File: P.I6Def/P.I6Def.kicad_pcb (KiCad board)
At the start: 2 copper layers, 48.9 x 70.8 mm, 41 parts, among them J1 B3B-PH-K-S, J2 B3B-PH-K-S, J3 CX90B-16P1, J4 B4B-PH-SM4-TB_LF__SN__P_, J5 B4B-PH-SM4-TB_LF__SN__P_, SW2 SW_SPST, SW3 SW_SPST, U2 LMV321IDCKT, U3 LMV321IDCKT, U4 LMV321IDCKT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

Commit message: MEJORA DE LA PCB
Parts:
- removed X1: ESP32-S3-WROOM-1-N16R8, ESP32-S3-WROOM-1-N16R8:ESP32S3WROOM1N8R2
- added U6: ESP32-S3-WROOM-1, RF_Module:ESP32-S3-WROOM-1U, F.Cu at (126.8, 93.2)
- moved C6 70.7 mm to (142.3, 81.1), turned to 180 degrees
- moved C16 65.1 mm to (139.0, 72.7)
- moved R7 60.4 mm to (142.2, 78.3), turned to 180 degrees
- moved C9 56.9 mm to (130.6, 72.0), turned to 90 degrees
- moved R8 51.5 mm to (132.9, 72.0), turned to 90 degrees
- moved C11 38.4 mm to (139.3, 98.4), turned to 0 degrees
- moved C5 37.8 mm to (139.4, 100.7), turned to 0 degrees
- moved R11 35.5 mm to (112.7, 96.9)
- moved R10 33.8 mm to (113.3, 80.6), turned to -90 degrees
- moved R9 30.1 mm to (111.2, 80.6), turned to -90 degrees
- moved SW3 19.1 mm to (123.1, 72.4), turned to 180 degrees
- moved J2 8.78 mm to (106.9, 70.0)
- moved J4 5.52 mm to (104.3, 82.3)
- moved J5 5.16 mm to (104.3, 95.8)
- moved SW2 3.30 mm to (142.5, 89.3), turned to -90 degrees
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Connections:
- net Net-(SW3-A) renamed /BOOT
- C1 pad 1: VBUS_B -> +5V
- C2 pad 1: VBUS_B -> +5V
- J3 pad B4: VBUS_B -> +5V
- J3 pad B9: VBUS_B -> +5V
- VR1 pad 1: VBUS_B -> +5V
- VR1 pad 4: VBUS_B -> +5V
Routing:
- net +3.3V: track 39.2 -> 164.0 mm, vias 1 -> 10
- net GND: track 109.2 -> 42.5 mm, vias 1 -> 3
- net /D-: track 0.00 -> 47.9 mm, vias 0 -> 4
- net /ADC1_CH1: track 1.92 -> 47.1 mm, vias 0 -> 2
- net /ADC1_CH0: track 0.00 -> 45.0 mm, vias 0 -> 4
- net /D+: track 0.00 -> 44.7 mm, vias 0 -> 4
- net Net-(SW2-A): track 0.00 -> 29.4 mm
- net +5V: track 47.4 -> 74.4 mm, vias 1 -> 2
- net /BOOT: track 0.00 -> 25.3 mm
- net /SCL_CSS811: track 0.00 -> 21.3 mm
- net VBUS_B: track 20.5 -> 0.00 mm
- net /SDA_CSS811: track 0.00 -> 19.5 mm, vias 0 -> 2
- net /ADDR_CCS811: track 0.00 -> 14.1 mm
- net /WAKE_CCS811: track 0.00 -> 12.2 mm
- net /nINT_CCS811: track 0.00 -> 11.8 mm
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- added copper zone on B.Cu, net GND
- added copper zone on F.Cu, net GND
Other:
- board size 48.9 x 70.8 mm -> 46.3 x 60.2 mm

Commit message: Actualizacion PCB
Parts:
- moved R11 1.53 mm to (112.4, 95.4)
- moved R12 0.90 mm to (121.7, 55.0)
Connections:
- U6 pad 17: unconnected-(U6-IO9-Pad17) -> /ADC1_CH0
- U6 pad 18: unconnected-(U6-IO10-Pad18) -> /ADC1_CH1
- U6 pad 4: /ADC1_CH1 -> unconnected-(U6-IO4-Pad4)
- U6 pad 5: /ADC1_CH0 -> unconnected-(U6-IO5-Pad5)
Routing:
- net GND: track 42.5 -> 73.2 mm, vias 3 -> 6
- net /ADC1_CH0: track 45.0 -> 25.5 mm, vias 4 -> 2
- net /ADC1_CH1: track 47.1 -> 29.1 mm
- net +5V: track 74.4 -> 62.5 mm
- net +3.3V: track 164.0 -> 174.0 mm
- net /D-: track 47.9 -> 55.0 mm
- net Net-(J5-Pad2): track 5.22 -> 6.03 mm
- net /ADDR_CCS811: track 14.1 -> 13.5 mm
- net Net-(U5-1IN-): track 13.4 -> 13.8 mm, vias 3 -> 0
- net Net-(U2-1IN+): track 6.44 -> 6.43 mm, vias 2 -> 0
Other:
- board size 46.3 x 60.2 mm -> 45.8 x 59.2 mm

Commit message: ACTUALIZACION DE LAS PISTAS DE LA PCB
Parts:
- moved J2 8.06 mm to (104.0, 62.5)
- moved R12 0.67 mm to (121.0, 55.0)
- moved SW2 0.50 mm to (142.0, 89.3)
- moved C12 0.32 mm to (134.0, 58.5), turned to 180 degrees
- moved R10 0.20 mm to (113.5, 80.6)
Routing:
- net GND: track 73.2 -> 5.66 mm, vias 6 -> 0
- net Net-(J2-Pad1): track 10.3 -> 3.72 mm
- net /D-: track 55.0 -> 52.7 mm
- net +5V: track 62.5 -> 60.5 mm
- net Net-(U5-1IN+): track 17.8 -> 19.3 mm
- net /D+: track 44.9 -> 43.4 mm
- net +3.3V: track 174.0 -> 172.9 mm
- net Net-(J3-CC2): track 3.00 -> 4.16 mm
- net /SCL_CSS811: track 21.3 -> 22.4 mm
- net Net-(J3-CC1): track 3.35 -> 4.01 mm
- removed copper zone on B.Cu, net GND
- removed copper zone on F.Cu, net GND

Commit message: Actualizacion PCB
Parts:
- added R14: 4.7k, ERA6AEB472V:RES_ERA6AEB472V, F.Cu at (112.4, 89.4)
- C16: value 0.1u -> 1uF; footprint C0805C104K8RACTU:CAPC2012X88N -> C2012X5R1C105K085AA:CAPC2012X100N
- R11: value 10k -> 4.7k; footprint MCU08050C1002FP500:RESC2012X55N -> ERA6AEB472V:RES_ERA6AEB472V
- moved C16 24.4 mm to (115.5, 66.2), turned to 180 degrees
- moved VR1 18.1 mm to (124.2, 60.8)
- moved C13 17.9 mm to (119.4, 60.9), turned to -90 degrees
- moved C2 17.8 mm to (128.9, 60.8), turned to -90 degrees
- moved C1 17.8 mm to (131.1, 60.8), turned to -90 degrees
- moved C10 17.2 mm to (117.0, 60.9), turned to -90 degrees
- moved J2 14.8 mm to (108.1, 48.3), turned to 0 degrees
- moved R11 13.9 mm to (110.7, 81.6), turned to 90 degrees
- moved C15 13.8 mm to (107.4, 61.7), turned to 180 degrees
- moved U4 12.2 mm to (107.5, 58.8)
- moved C7 11.9 mm to (107.4, 56.1), turned to 0 degrees
- moved R6 11.5 mm to (107.4, 53.9), turned to 180 degrees
- moved R5 9.51 mm to (112.1, 53.0), turned to -90 degrees
- moved R9 9.07 mm to (112.3, 71.6)
- moved R10 9.02 mm to (114.4, 71.6)
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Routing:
- net +3.3V: track 172.9 -> 82.4 mm, vias 10 -> 4
- net /D-: track 52.7 -> 2.36 mm, vias 4 -> 0
- net /D+: track 43.4 -> 2.76 mm, vias 4 -> 0
- net /ADC1_CH1: track 29.3 -> 1.92 mm, vias 2 -> 0
- net /ADC1_CH0: track 25.5 -> 1.92 mm, vias 2 -> 0
- net Net-(SW2-A): track 30.2 -> 16.2 mm
- net +5V: track 60.5 -> 70.7 mm
- net Net-(U5-1IN-): track 14.1 -> 5.09 mm
- net Net-(U5-1IN+): track 19.3 -> 12.1 mm, vias 2 -> 0
- net Net-(J5-Pad2): track 5.85 -> 11.4 mm, vias 0 -> 2
- net Net-(U3-1IN-): track 4.47 -> 9.40 mm
- net /BOOT: track 25.3 -> 21.2 mm, vias 0 -> 2
- net Net-(J2-Pad1): track 3.72 -> 7.10 mm
- net /nINT_CCS811: track 12.2 -> 9.72 mm
- net Net-(U3-1IN+): track 4.99 -> 7.34 mm
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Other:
- board size 45.8 x 59.2 mm -> 45.9 x 52.7 mm

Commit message: terminar conecciones y reorganizar los componentes
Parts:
- moved C11 7.79 mm to (144.5, 94.4), turned to -90 degrees
- moved C12 7.51 mm to (143.5, 57.0)
- moved R14 5.12 mm to (112.0, 94.5), turned to 0 degrees
- moved R3 4.88 mm to (144.5, 62.0)
- moved U4 4.85 mm to (105.0, 63.0)
- moved C14 4.36 mm to (140.5, 68.5)
- moved C8 3.18 mm to (141.5, 62.0)
- moved U2 3.02 mm to (139.0, 65.5)
- moved R7 2.86 mm to (136.0, 74.5), turned to -90 degrees
- moved R12 2.72 mm to (118.5, 56.0)
- moved C15 2.72 mm to (109.0, 59.5), turned to 90 degrees
- moved R8 2.12 mm to (132.0, 71.5), turned to 90 degrees
- moved C9 2.06 mm to (129.5, 71.5), turned to 90 degrees
- moved C16 2.01 mm to (113.5, 66.0)
- moved C6 1.88 mm to (140.0, 74.5), turned to 90 degrees
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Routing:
- net +3.3V: track 82.4 -> 164.5 mm, vias 4 -> 8
- net /D-: track 2.36 -> 41.3 mm, vias 0 -> 2
- net /D+: track 2.76 -> 40.2 mm, vias 0 -> 2
- net /ADC1_CH1: track 1.92 -> 38.7 mm, vias 0 -> 2
- net /ADC1_CH0: track 1.92 -> 34.1 mm, vias 0 -> 2
- net Net-(SW2-A): track 16.2 -> 25.5 mm
- net /nINT_CCS811: track 9.72 -> 16.9 mm, vias 0 -> 2
- net Net-(U4-1IN+): track 4.34 -> 10.4 mm
- net Net-(U5-1IN-): track 5.09 -> 10.1 mm
- net Net-(U5-1IN+): track 12.1 -> 7.39 mm
- net Net-(J3-CC2): track 4.16 -> 8.68 mm, vias 0 -> 2
- net Net-(J5-Pad2): track 11.4 -> 14.2 mm
- net Net-(J1-Pad1): track 6.11 -> 3.96 mm
- net Net-(U2-1IN+): track 8.57 -> 10.7 mm
- net /ADDR_CCS811: track 12.3 -> 10.3 mm
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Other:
- board size 45.9 x 52.7 mm -> 46.1 x 52.7 mm

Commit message: Relleno de Cobre
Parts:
- moved C11 5.50 mm to (139.0, 94.6)
- moved C12 3.61 mm to (140.1, 55.8)
- moved R2 3.11 mm to (136.9, 53.2)
- moved C5 2.60 mm to (136.4, 94.6)
- moved C15 2.55 mm to (106.5, 60.0), turned to 180 degrees
- moved R1 1.91 mm to (134.1, 53.1)
- moved C6 1.50 mm to (138.5, 74.5)
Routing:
- net Net-(J1-Pad1): track 3.96 -> 6.80 mm
- net +3.3V: track 164.5 -> 167.2 mm, vias 8 -> 7
- net /ADC1_CH0: track 34.1 -> 31.7 mm
- net Net-(J5-Pad2): track 14.2 -> 12.4 mm
- net Net-(SW2-A): track 25.5 -> 24.0 mm
- net Net-(U5-1IN+): track 7.39 -> 8.23 mm
- net GND: track 4.55 -> 4.69 mm, vias 0 -> 5
- added copper zone on B.Cu, net GND
- added copper zone on F.Cu, net GND

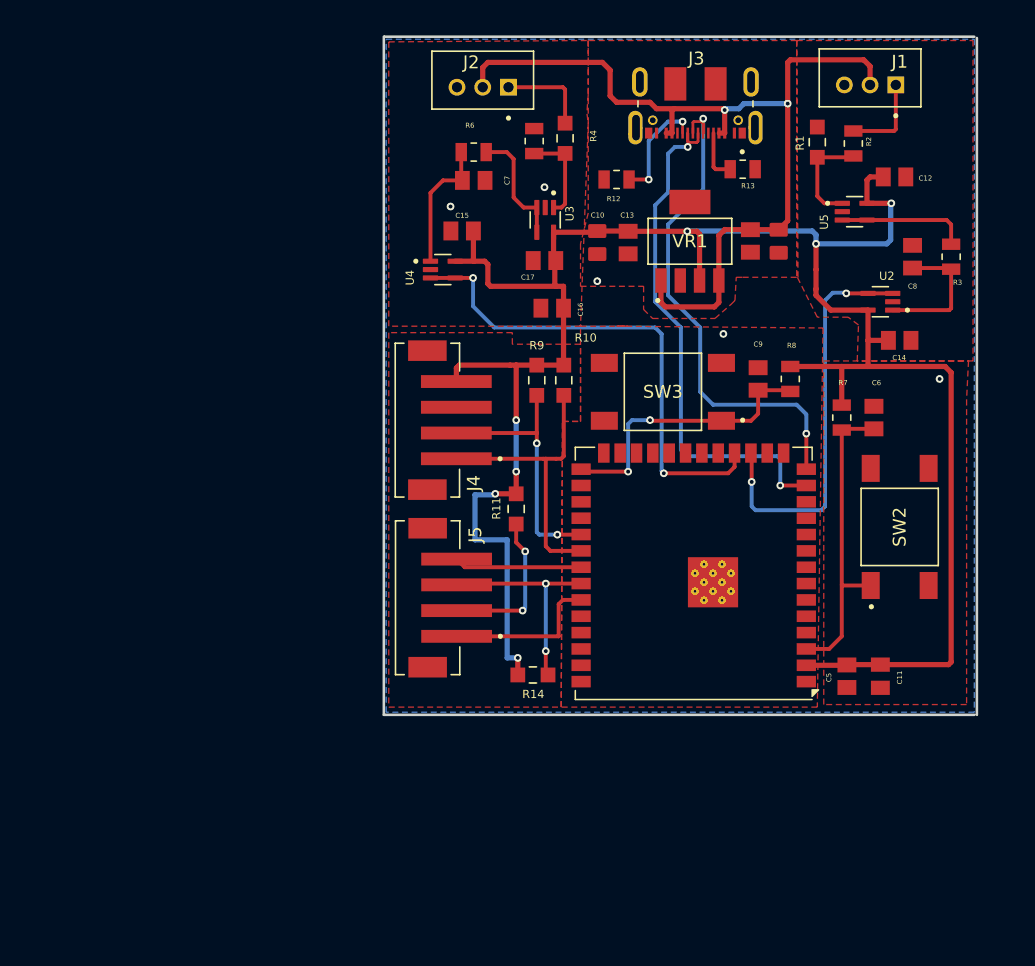
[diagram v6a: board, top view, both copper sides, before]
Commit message: Solucion de errores y advertencias de DRC
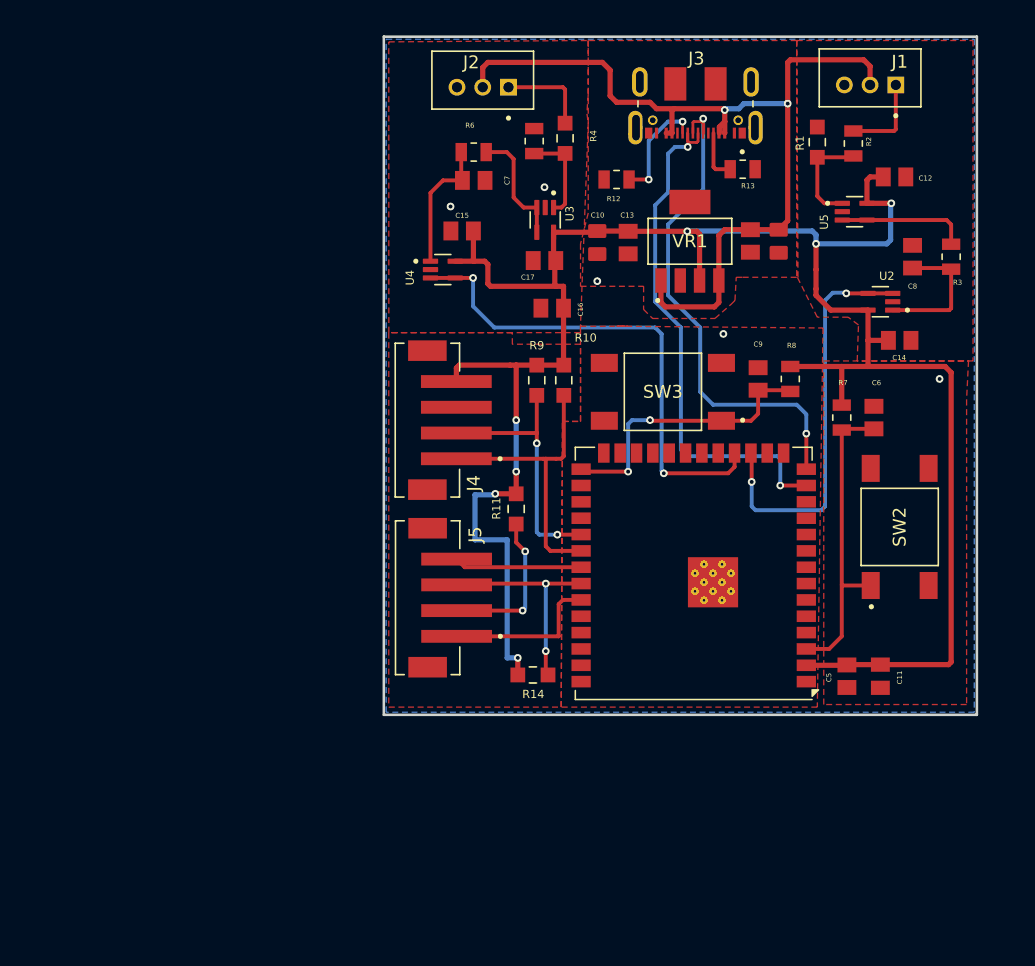
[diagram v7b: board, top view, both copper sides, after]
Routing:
- net +5V: track 70.7 -> 71.3 mm
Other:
- outline, holes or cut-outs redrawn
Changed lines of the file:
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@@
 	)
 	(setup
+		(stackup
+			(layer "F.SilkS"
+				(type "Top Silk Screen")
+			)
+			(layer "F.Paste"
+				(type "Top Solder Paste")
+			)
+			(layer "F.Mask"
+				(type "Top Solder Mask")
+				(thickness 0.01)
+			)
+			(layer "F.Cu"
+				(type "copper")
+				(thickness 0.035)
+			)
+			(layer "dielectric 1"
+				(type "core")
+				(thickness 1.51)
+				(material "FR4")
+				(epsilon_r 4.5)
+				(loss_tangent 0.02)
+			)
+			(layer "B.Cu"
+				(type "copper")
+				(thickness 0.035)
+			)
+			(layer "B.Mask"
+				(type "Bottom Solder Mask")
+				(thickness 0.01)
+			)
+			(layer "B.Paste"
+				(type "Bottom Solder Paste")
+			)
+			(layer "B.SilkS"
+				(type "Bottom Silk Screen")
+			)
+			(copper_finish "None")
+			(dielectric_constraints no)
+		)
 		(pad_to_mask_clearance 0)
 		(allow_soldermask_bridges_in_footprints no)
@@
 	)
 	(gr_line
-		(start 100.415221 97.6)
-		(end 100.415221 44.901473)
+		(start 100.415221 44.901506)
+		(end 146.5 44.901506)
 		(stroke
 			(width 0.2)
@@
 	)
 	(gr_line
-		(start 100.474963 44.901506)
-		(end 146.300441 44.901506)
+		(start 100.415221 97.6)
+		(end 100.415221 44.901473)
 		(stroke
 			(width 0.2)
@@
 	)
 	(gr_line
-		(start 146.3 97.6)
-		(end 100.415221 97.6)
+		(start 146.5 44.901506)
+		(end 146.5 97.600945)
 		(stroke
 			(width 0.2)
@@
 	)
 	(gr_line
-		(start 146.5 45)
-		(end 146.5 97.600945)
+		(start 146.5 97.600945)
+		(end 100.415221 97.6)
 		(stroke
 			(width 0.2)
@@
 	)
 	(segment
-		(start 133.875 64.625)
-		(end 134 64.5)
-		(width 0.2)
-		(layer "F.Cu")
-		(net "+3.3V")
-	)
-	(segment
 		(start 113.7 64.2)
 		(end 113.8 64.3)
@@
 	)
 	(segment
+		(start 126.48895 51.9178)
+		(end 126.48895 52.395)
+		(width 0.4064)
+		(layer "F.Cu")
+		(net "+5V")
+	)
+	(segment
 		(start 131.8 50.1)
 		(end 131.8 59.205)
@@
 	)
 	(segment
+		(start 126.90675 51.5)
+		(end 126.90675 52.3815)
+		(width 0.4064)
+		(layer "F.Cu")
+		(net "+5V")
+	)
+	(segment
+		(start 126.90675 52.3815)
+		(end 126.9 52.38825)
+		(width 0.4064)
+		(layer "F.Cu")
+		(net "+5V")
+	)
+	(segment
 		(start 138.2 47.2)
 		(end 138.2 48.65)
@@
 	)
 	(segment
-		(start 126.9 50.6)
-		(end 126.9 52.38825)
-		(width 0.4064)
-		(layer "F.Cu")
-		(net "+5V")
-	)
-	(segment
 		(start 123 50.5)
 		(end 126.8 50.5)
@@
 	)
 	(segment
-		(start 126.90675 52.395)
-		(end 126.48415 52.395)
-		(width 0.4064)
-		(layer "F.Cu")
-		(net "+5V")
-	)
-	(segment
 		(start 132 46.7)
 		(end 137.7 46.7)
@@
 	)
 	(segment
-		(start 126.9 59.9)
-		(end 126.92 59.88)
+		(start 126.90675 50.60675)
+		(end 126.90675 51.5)
 		(width 0.4064)
 		(layer "F.Cu")
@@
 	)
 	(segment
+		(start 126.90675 51.5)
+		(end 126.48895 51.9178)
+		(width 0.4064)
+		(layer "F.Cu")
+		(net "+5V")
+	)
+	(segment
 		(start 128.9 59.9)
 		(end 131.095 59.9)
@@
 	)
 	(segment
+		(start 126.9 50.6)
+		(end 126.90675 50.60675)
+		(width 0.4064)
+		(layer "F.Cu")
+		(net "+5V")
+	)
+	(segment
 		(start 118.5 50)
 		(end 118 49.5)
@@
 		(polygon
 			(pts
-				(xy 116.3 47.375001) (xy 116.3 49.4) (xy 116.238789 50.156009) (xy 116.2 50.9) (xy 116.3 51.6) (xy 115.7 67.4)
-				(xy 100.8 67.4) (xy 100.8 45.305442) (xy 116.3 45.2) (xy 116.296963 45.763932)
+				(xy 116.3 47.375001) (xy 116.3 49.4) (xy 116.238789 50.156009) (xy 116.2 50.9) (xy 116.3 51.6) (xy 115.677145 67.9)
+				(xy 100.803851 67.9) (xy 100.8 45.305442) (xy 116.3 45.2) (xy 116.296963 45.763932)
 			)
 		)

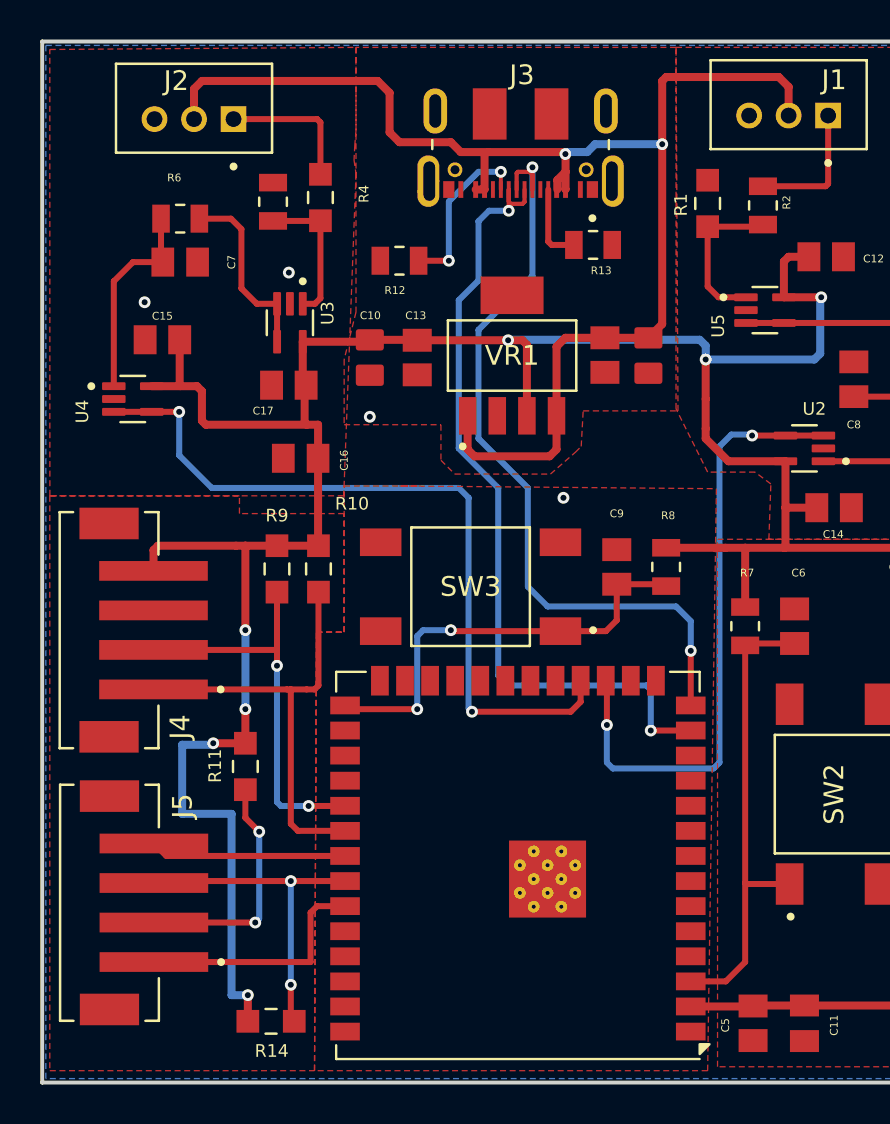
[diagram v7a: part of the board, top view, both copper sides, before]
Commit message: fix: correcciones de DRC - falta corregir alivios term y 45grad
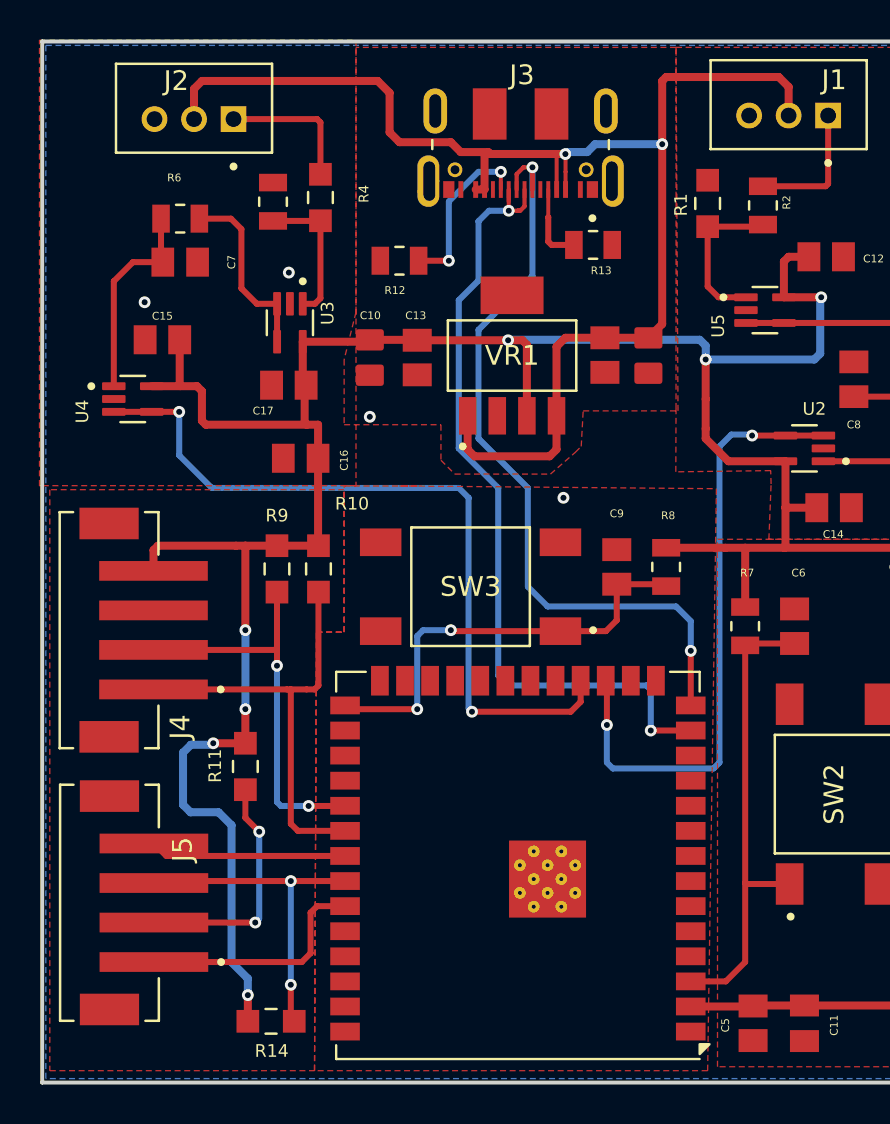
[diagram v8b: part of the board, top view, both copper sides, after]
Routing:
- net +3.3V: track 167.0 -> 165.6 mm
- net +5V: track 71.3 -> 72.1 mm
